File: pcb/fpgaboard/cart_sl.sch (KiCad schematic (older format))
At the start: 35 parts, among them J16 CONN_02X16, J17 CONN_02X16, J18 CONN_02X16, J19 CONN_02X03, Q2 BSS138, U12 74LVCH8T245, U13 74LVCH8T245, U14 74LVCH8T245, U15 74LVCH8T245

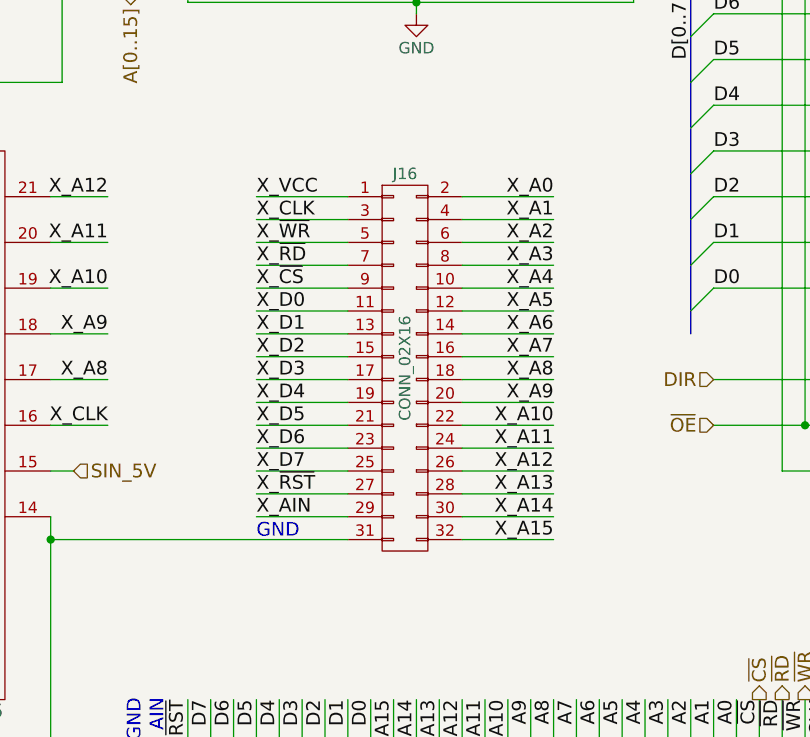
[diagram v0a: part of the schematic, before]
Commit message: fix pin swap of gbreveng fpga board J16
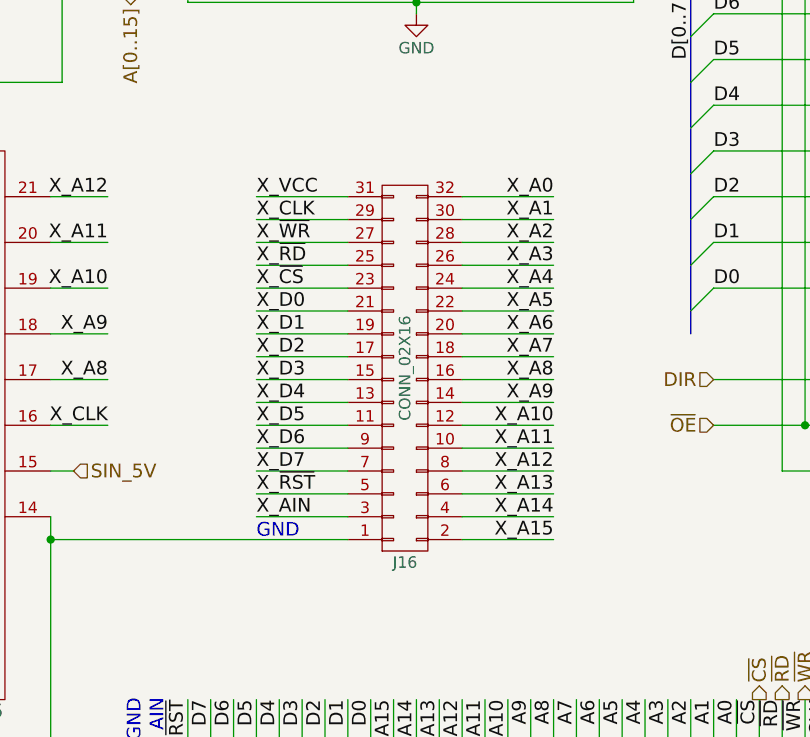
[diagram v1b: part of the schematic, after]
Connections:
- net GND: now also J16.1 (P1); no longer J16.31 (P31)
- net X_A0: now also J16.32 (P32); no longer J16.2 (P2)
- net X_A1: now also J16.30 (P30); no longer J16.4 (P4)
- net X_A10: now also J16.12 (P12); no longer J16.22 (P22)
- net X_A11: now also J16.10 (P10); no longer J16.24 (P24)
- net X_A12: now also J16.8 (P8); no longer J16.26 (P26)
- net X_A13: now also J16.6 (P6); no longer J16.28 (P28)
- net X_A14: now also J16.4 (P4); no longer J16.30 (P30)
- net X_A15: now also J16.2 (P2); no longer J16.32 (P32)
- net X_A2: now also J16.28 (P28); no longer J16.6 (P6)
- net X_A3: now also J16.26 (P26); no longer J16.8 (P8)
- net X_A4: now also J16.24 (P24); no longer J16.10 (P10)
- net X_A5: now also J16.22 (P22); no longer J16.12 (P12)
- net X_A6: now also J16.20 (P20); no longer J16.14 (P14)
- net X_A7: now also J16.18 (P18); no longer J16.16 (P16)
- net X_A8: now also J16.16 (P16); no longer J16.18 (P18)
- net X_A9: now also J16.14 (P14); no longer J16.20 (P20)
- net X_AIN: now also J16.3 (P3); no longer J16.29 (P29)
- net X_CLK: now also J16.29 (P29); no longer J16.3 (P3)
- net X_D0: now also J16.21 (P21); no longer J16.11 (P11)
- net X_D1: now also J16.19 (P19); no longer J16.13 (P13)
- net X_D2: now also J16.17 (P17); no longer J16.15 (P15)
- net X_D3: now also J16.15 (P15); no longer J16.17 (P17)
- net X_D4: now also J16.13 (P13); no longer J16.19 (P19)
- net X_D5: now also J16.11 (P11); no longer J16.21 (P21)
- net X_D6: now also J16.9 (P9); no longer J16.23 (P23)
- net X_D7: now also J16.7 (P7); no longer J16.25 (P25)
- net X_VCC: now also J16.31 (P31); no longer J16.1 (P1)
- net X_~CS: now also J16.23 (P23); no longer J16.9 (P9)
- net X_~RD: now also J16.25 (P25); no longer J16.7 (P7)
- net X_~RST: now also J16.5 (P5); no longer J16.27 (P27)
- net X_~WR: now also J16.27 (P27); no longer J16.5 (P5)
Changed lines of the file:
@@
 LIBS:tda7050
 LIBS:Connector
-LIBS:SeeedOPL-Connector-2016
 LIBS:fpgaboard-cache
 EELAYER 25 0
@@
 Sheet 8 11
 Title "Game Boy reverse eng. FPGA board"
-Date "2019-01-20"
-Rev "0"
+Date "2019-08-11"
+Rev "1"
 Comp "Author: Michael Singer"
 Comment1 "https://sourceforge.net/projects/iceboy/"
@@
 F 3 "" H 4350 4450 50  0001 C CNN
 	1    4350 5550
-	1    0    0    -1
+	1    0    0    1
 $EndComp
 Text Label 7500 1600 1    60   ~ 0

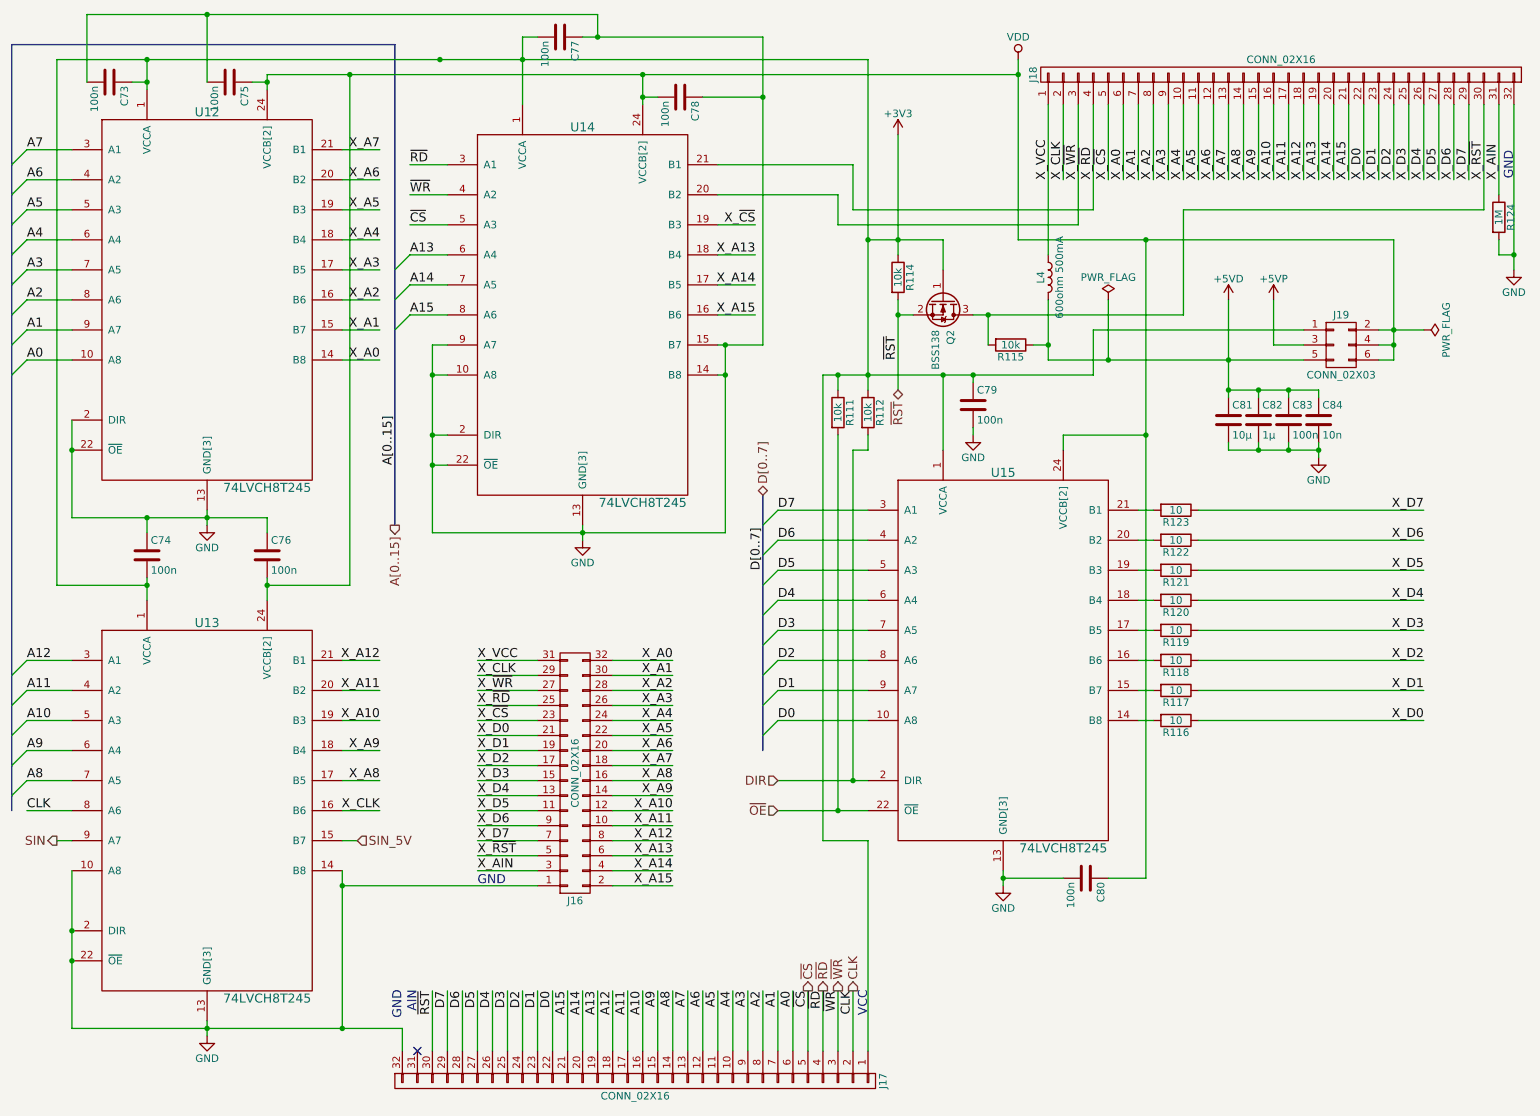
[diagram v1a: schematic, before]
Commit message: label all external connector pins on gbreveng brd.
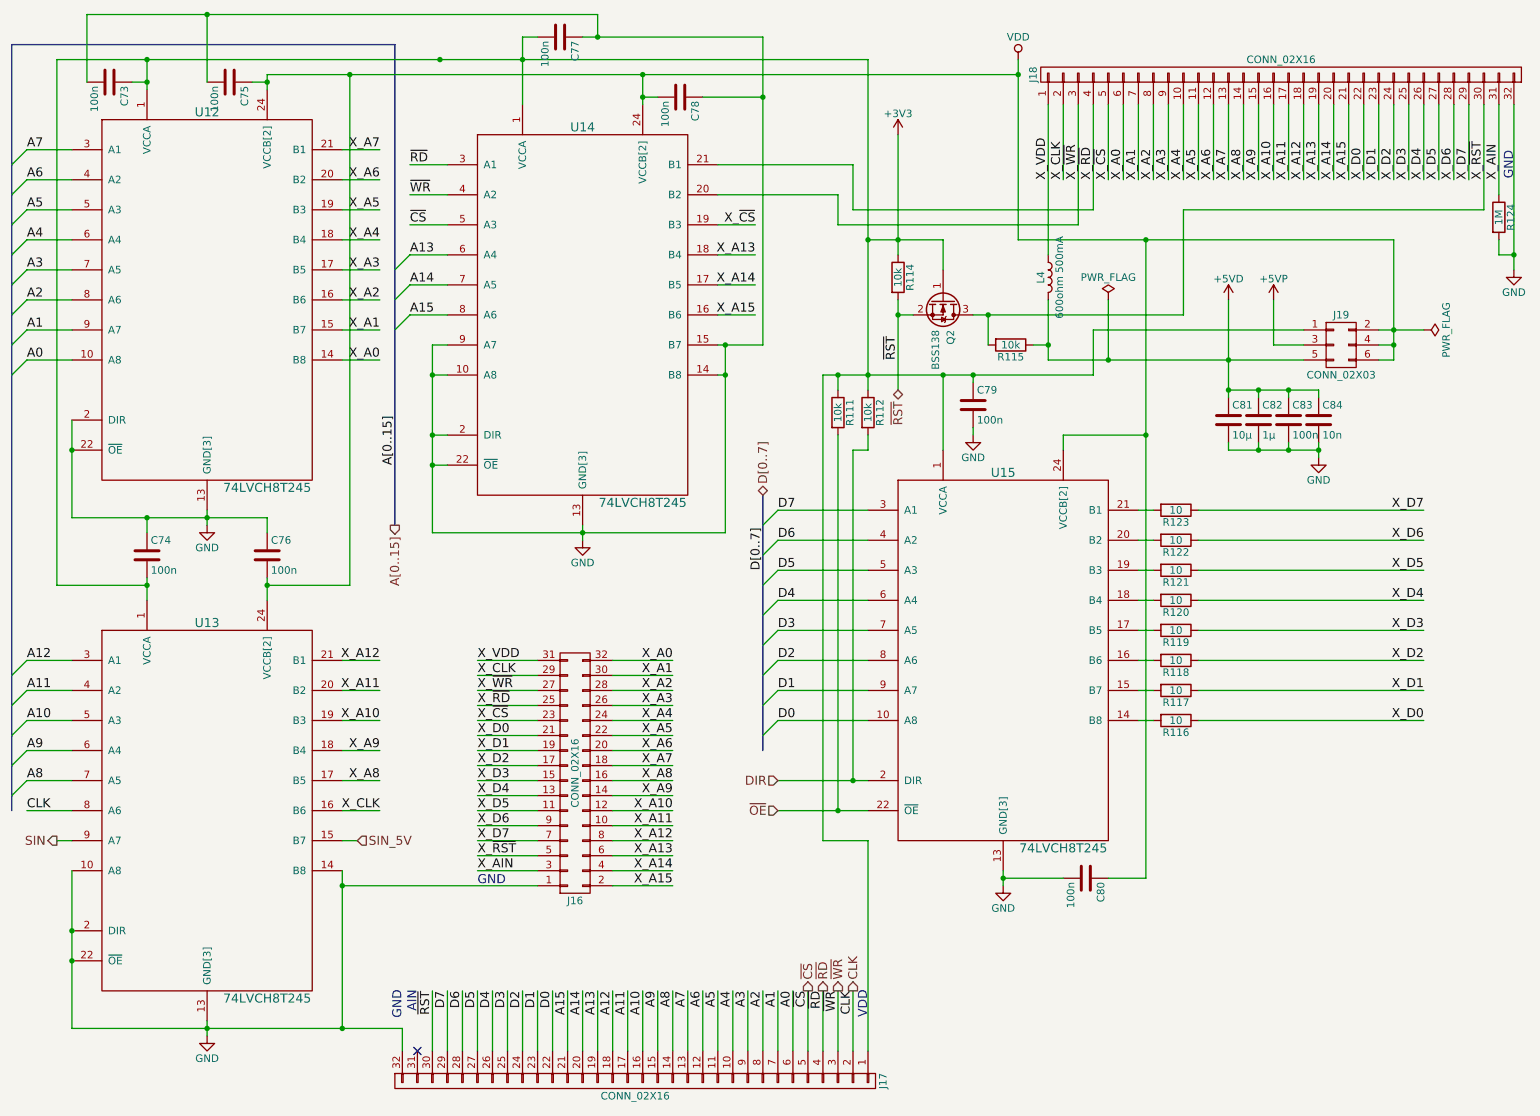
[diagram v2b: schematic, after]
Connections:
- net X_VCC renamed X_VDD
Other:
- note added: "VDD"
- note removed: "VCC"
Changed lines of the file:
@@
 Sheet 8 11
 Title "Game Boy reverse eng. FPGA board"
-Date "2019-08-11"
+Date "2019-08-17"
 Rev "1"
 Comp "Author: Michael Singer"
@@
 	3400 7000 3400 7400
 Text Notes 6300 7000 3    60   ~ 0
-VCC
+VDD
 Text Notes 3200 7000 3    60   ~ 0
 GND
@@
 $EndComp
 Text Label 7500 1600 1    60   ~ 0
-X_VCC
+X_VDD
 Text Label 3700 4800 0    60   ~ 0
-X_VCC
+X_VDD
 Text Label 3700 4900 0    60   ~ 0
 X_CLK
